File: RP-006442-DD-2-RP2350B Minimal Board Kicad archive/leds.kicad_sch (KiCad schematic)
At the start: 1 part

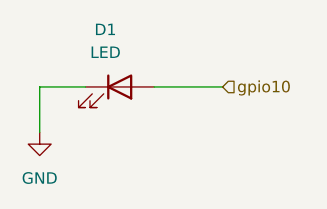
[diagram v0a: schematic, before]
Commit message: Placed hierarchical labels in debugprobe
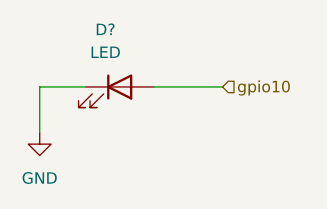
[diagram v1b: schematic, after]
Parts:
- renumbered D1 to D?
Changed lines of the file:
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@@
 		(dnp no)
 		(fields_autoplaced yes)
-		(property "Reference" "D1"
+		(property "Reference" "D?"
 			(at 141.9225 93.98 0)
 			(effects
@@
 		)
 		(instances
-			(project ""
-				(path "/94683f5c-9cd9-448e-be96-9792537b5cb8/9cbf39f9-c028-4bb9-9381-26efe67c51db"
-					(reference "D1")
+			(project "RP2350_80QFN_minimal"
+				(path "/94683f5c-9cd9-448e-be96-9792537b5cb8/c2516de1-a5e0-487a-9315-df4770cb259d"
+					(reference "D?")
 					(unit 1)
 				)
@@
 		(dnp no)
 		(fields_autoplaced yes)
-		(property "Reference" "#PWR066"
+		(property "Reference" "#PWR?"
 			(at 134.62 111.76 0)
 			(effects
@@
 		)
 		(instances
-			(project ""
-				(path "/94683f5c-9cd9-448e-be96-9792537b5cb8/9cbf39f9-c028-4bb9-9381-26efe67c51db"
-					(reference "#PWR066")
+			(project "RP2350_80QFN_minimal"
+				(path "/94683f5c-9cd9-448e-be96-9792537b5cb8/c2516de1-a5e0-487a-9315-df4770cb259d"
+					(reference "#PWR?")
 					(unit 1)
 				)

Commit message: Assigned footprints to symbols
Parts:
- removed D?: LED, LED_SMD:LED_0402_1005Metric, symbol Device:LED
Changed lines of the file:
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@@
 	(generator_version "9.0")
 	(paper "A4")
-	(wire
-		(pts
-			(xy 154.94 100.33) (xy 147.32 100.33)
-		)
-		(stroke
-			(width 0)
-			(type default)
-		)
-	)
-	(wire
-		(pts
-			(xy 134.62 105.41) (xy 134.62 100.33)
-		)
-		(stroke
-			(width 0)
-			(type default)
-		)
-	)
-	(wire
-		(pts
-			(xy 134.62 100.33) (xy 139.7 100.33)
-		)
-		(stroke
-			(width 0)
-			(type default)
-		)
-	)
-	(hierarchical_label "gpio10"
-		(shape input)
-		(at 154.94 100.33 0)
-		(effects
-			(font
-				(size 1.27 1.27)
-			)
-			(justify left)
-		)
-	)
-	(symbol
-		(lib_id "Device:LED")
-		(at 143.51 100.33 0)
-		(unit 1)
-		(exclude_from_sim no)
-		(in_bom yes)
-		(on_board yes)
-		(dnp no)
-		(fields_autoplaced yes)
-		(property "Reference" "D?"
-			(at 141.9225 93.98 0)
-			(effects
-				(font
-					(size 1.27 1.27)
-				)
-			)
-		)
-		(property "Value" "LED"
-			(at 141.9225 96.52 0)
-			(effects
-				(font
-					(size 1.27 1.27)
-				)
-			)
-		)
-		(property "Footprint" "LED_SMD:LED_0402_1005Metric"
-			(at 143.51 100.33 0)
-			(effects
-				(font
-					(size 1.27 1.27)
-				)
-				(hide yes)
-			)
-		)
-		(property "Datasheet" "~"
-			(at 143.51 100.33 0)
-			(effects
-				(font
-					(size 1.27 1.27)
-				)
-				(hide yes)
-			)
-		)
-		(property "Description" "Light emitting diode"
-			(at 143.51 100.33 0)
-			(effects
-				(font
-					(size 1.27 1.27)
-				)
-				(hide yes)
-			)
-		)
-		(property "Sim.Pins" "1=K 2=A"
-			(at 143.51 100.33 0)
-			(effects
-				(font
-					(size 1.27 1.27)
-				)
-				(hide yes)
-			)
-		)
-		(pin "1"
-		)
-		(pin "2"
-		)
-		(instances
-			(project "RP2350_80QFN_minimal"
-				(path "/94683f5c-9cd9-448e-be96-9792537b5cb8/c2516de1-a5e0-487a-9315-df4770cb259d"
-					(reference "D?")
-					(unit 1)
-				)
-			)
-		)
-	)
-	(symbol
-		(lib_id "power:GND")
-		(at 134.62 105.41 0)
-		(unit 1)
-		(exclude_from_sim no)
-		(in_bom yes)
-		(on_board yes)
-		(dnp no)
-		(fields_autoplaced yes)
-		(property "Reference" "#PWR?"
-			(at 134.62 111.76 0)
-			(effects
-				(font
-					(size 1.27 1.27)
-				)
-				(hide yes)
-			)
-		)
-		(property "Value" "GND"
-			(at 134.62 110.49 0)
-			(effects
-				(font
-					(size 1.27 1.27)
-				)
-			)
-		)
-		(property "Footprint" ""
-			(at 134.62 105.41 0)
-			(effects
-				(font
-					(size 1.27 1.27)
-				)
-				(hide yes)
-			)
-		)
-		(property "Datasheet" ""
-			(at 134.62 105.41 0)
-			(effects
-				(font
-					(size 1.27 1.27)
-				)
-				(hide yes)
-			)
-		)
-		(property "Description" "Power symbol creates a global label with name \"GND\" , ground"
-			(at 134.62 105.41 0)
-			(effects
-				(font
-					(size 1.27 1.27)
-				)
-				(hide yes)
-			)
-		)
-		(pin "1"
-		)
-		(instances
-			(project "RP2350_80QFN_minimal"
-				(path "/94683f5c-9cd9-448e-be96-9792537b5cb8/c2516de1-a5e0-487a-9315-df4770cb259d"
-					(reference "#PWR?")
-					(unit 1)
-				)
-			)
-		)
-	)
 )

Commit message: added led symbol
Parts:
- added D1: LED, LED_SMD:LED_0402_1005Metric, symbol Device:LED
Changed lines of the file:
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@@
 	(generator_version "9.0")
 	(paper "A4")
+	(symbol
+		(lib_id "Device:LED")
+		(at 143.51 100.33 0)
+		(unit 1)
+		(exclude_from_sim no)
+		(in_bom yes)
+		(on_board yes)
+		(dnp no)
+		(fields_autoplaced yes)
+		(property "Reference" "D1"
+			(at 141.9225 93.98 0)
+			(effects
+				(font
+					(size 1.27 1.27)
+				)
+			)
+		)
+		(property "Value" "LED"
+			(at 141.9225 96.52 0)
+			(effects
+				(font
+					(size 1.27 1.27)
+				)
+			)
+		)
+		(property "Footprint" "LED_SMD:LED_0402_1005Metric"
+			(at 143.51 100.33 0)
+			(effects
+				(font
+					(size 1.27 1.27)
+				)
+				(hide yes)
+			)
+		)
+		(property "Datasheet" "~"
+			(at 143.51 100.33 0)
+			(effects
+				(font
+					(size 1.27 1.27)
+				)
+				(hide yes)
+			)
+		)
+		(property "Description" "Light emitting diode"
+			(at 143.51 100.33 0)
+			(effects
+				(font
+					(size 1.27 1.27)
+				)
+				(hide yes)
+			)
+		)
+		(property "Sim.Pins" "1=K 2=A"
+			(at 143.51 100.33 0)
+			(effects
+				(font
+					(size 1.27 1.27)
+				)
+				(hide yes)
+			)
+		)
+		(pin "1"
+		)
+		(pin "2"
+		)
+		(instances
+			(project ""
+				(path "/94683f5c-9cd9-448e-be96-9792537b5cb8/9cbf39f9-c028-4bb9-9381-26efe67c51db"
+					(reference "D1")
+					(unit 1)
+				)
+			)
+		)
+	)
 )
